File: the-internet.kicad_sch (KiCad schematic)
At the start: 10 parts, among them J1 POWER, J2 LOLIN-C3-MINI (L), J3 LOLIN-C3-MINI (R), Q1 DMP2004K, Q2 DMP2004K

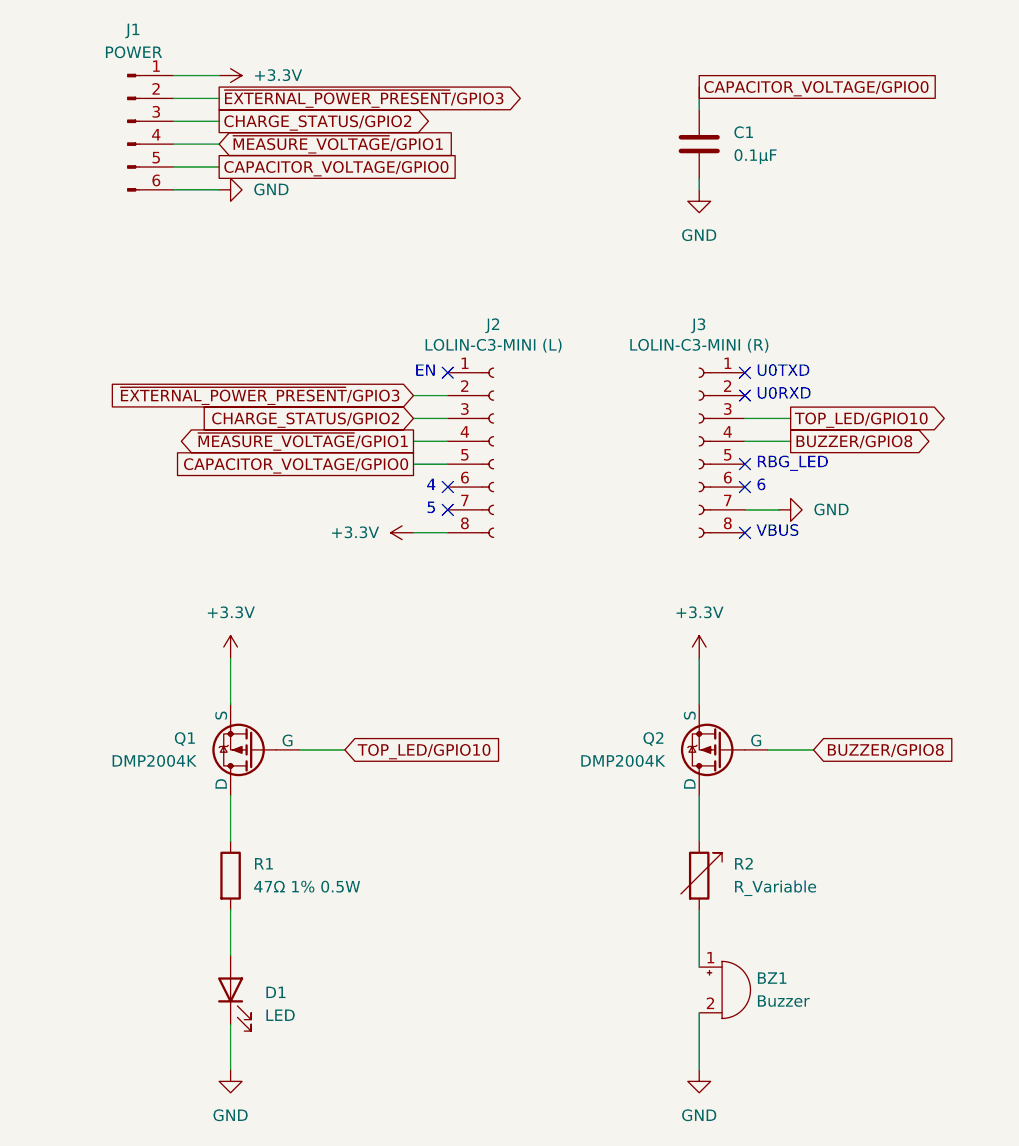
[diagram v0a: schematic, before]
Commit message: Remove ADC divider control
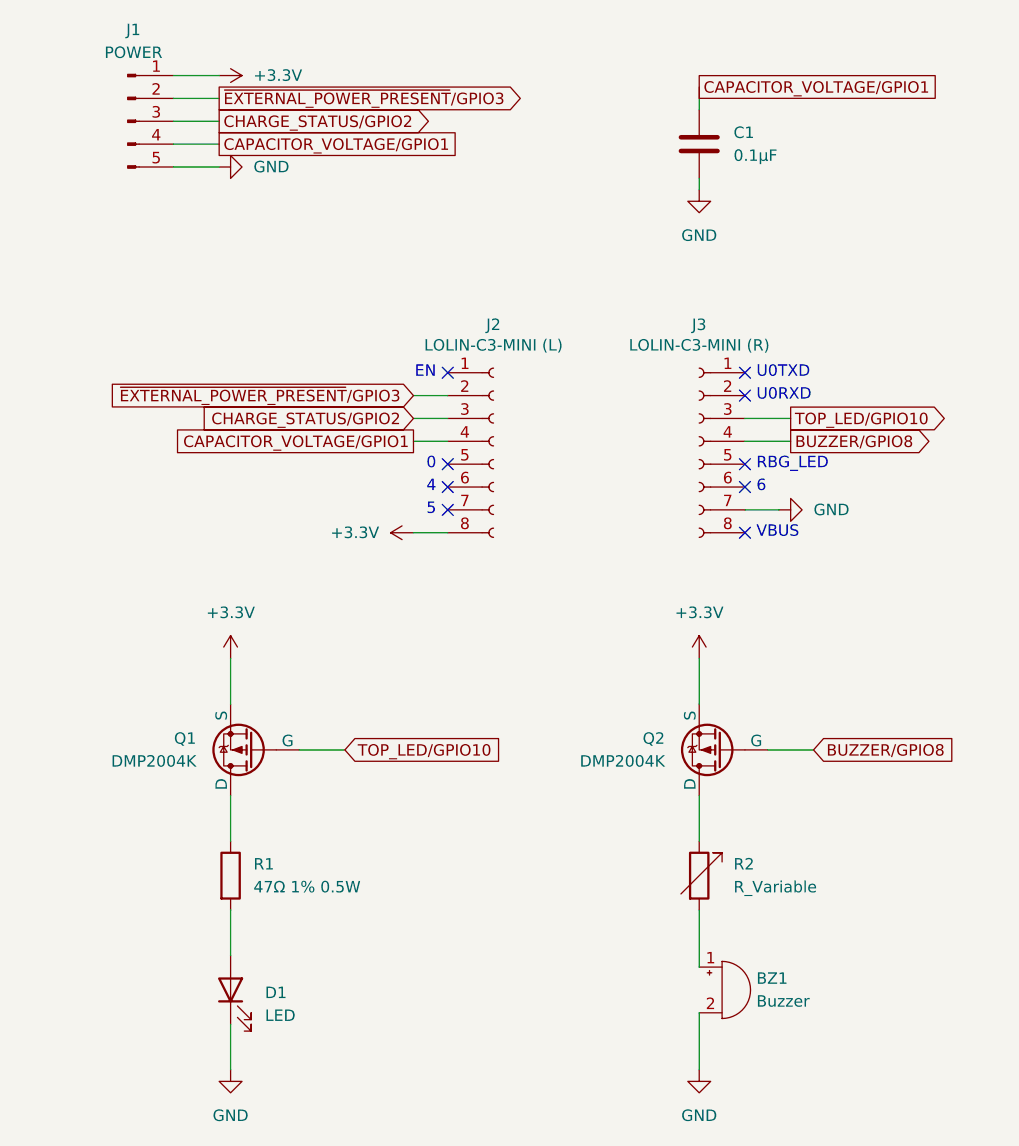
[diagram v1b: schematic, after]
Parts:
- J1: footprint Connector_PinHeader_2.54mm:PinHeader_1x06_P2.54mm_Vertical -> Connector_PinHeader_2.54mm:PinHeader_1x05_P2.54mm_Vertical; symbol Connector:Conn_01x06_Pin -> Connector:Conn_01x05_Pin
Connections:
- net GND: now also J1.5 (Pin_5); no longer J1.6 (Pin_6)
- removed net CAPACITOR_VOLTAGE/GPIO0: C1.1, J1.5 (Pin_5), J2.5 (Pin_5)
- net ~{MEASURE_VOLTAGE}/GPIO1 renamed CAPACITOR_VOLTAGE/GPIO1
- net CAPACITOR_VOLTAGE/GPIO1: now also C1.1
- no-connect marks 8 -> 9
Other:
- note added: "0"
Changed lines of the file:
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@@
+		)
+	)
+	(text "0"
+		(exclude_from_sim no)
+		(at 43.18 57.15 0)
+		(effects
+			(font
+				(size 1.27 1.27)
+			)
+			(justify right)
 		)
 	)
@@
 		(at 77.47 59.69)
 	)
+	(no_connect
+		(at 44.45 57.15)
+	)
 	(wire
 		(pts
@@
 	(wire
 		(pts
-			(xy 13.97 26.67) (xy 19.05 26.67)
-		)
-		(stroke
-			(width 0)
-			(type default)
-		)
-	)
-	(wire
-		(pts
 			(xy 77.47 54.61) (xy 82.55 54.61)
 		)
@@
 	(wire
 		(pts
-			(xy 40.64 57.15) (xy 44.45 57.15)
-		)
-		(stroke
-			(width 0)
-			(type default)
-		)
-	)
-	(wire
-		(pts
 			(xy 20.32 119.38) (xy 20.32 124.46)
 		)
@@
 		)
 	)
-	(global_label "CAPACITOR_VOLTAGE{slash}GPIO0"
+	(global_label "CAPACITOR_VOLTAGE{slash}GPIO1"
 		(shape passive)
 		(at 72.39 15.24 0)
@@
 		)
 	)
-	(global_label "CAPACITOR_VOLTAGE{slash}GPIO0"
+	(global_label "CAPACITOR_VOLTAGE{slash}GPIO1"
 		(shape passive)
-		(at 19.05 24.13 0)
+		(at 19.05 21.59 0)
 		(fields_autoplaced yes)
 		(effects
@@
 		)
 		(property "Intersheetrefs" "${INTERSHEET_REFS}"
-			(at 46.9893 24.13 0)
-			(effects
-				(font
-					(size 1.27 1.27)
-				)
-				(justify left)
-				(hide yes)
-			)
-		)
-	)
-	(global_label "CAPACITOR_VOLTAGE{slash}GPIO0"
+			(at 46.9893 21.59 0)
+			(effects
+				(font
+					(size 1.27 1.27)
+				)
+				(justify left)
+				(hide yes)
+			)
+		)
+	)
+	(global_label "CAPACITOR_VOLTAGE{slash}GPIO1"
 		(shape passive)
-		(at 40.64 57.15 180)
+		(at 40.64 54.61 180)
 		(fields_autoplaced yes)
 		(effects
@@
 		)
 		(property "Intersheetrefs" "${INTERSHEET_REFS}"
-			(at 12.7007 57.15 0)
+			(at 12.7007 54.61 0)
 			(effects
 				(font
@@
 				)
 				(justify right)
-				(hide yes)
-			)
-		)
-	)
-	(global_label "~{MEASURE_VOLTAGE}{slash}GPIO1"
-		(shape output)
-		(at 40.64 54.61 180)
-		(fields_autoplaced yes)
-		(effects
-			(font
-				(size 1.27 1.27)
-			)
-			(justify right)
-		)
-		(property "Intersheetrefs" "${INTERSHEET_REFS}"
-			(at 13.1015 54.61 0)
-			(effects
-				(font
-					(size 1.27 1.27)
-				)
-				(justify right)
-				(hide yes)
-			)
-		)
-	)
-	(global_label "~{MEASURE_VOLTAGE}{slash}GPIO1"
-		(shape input)
-		(at 19.05 21.59 0)
-		(fields_autoplaced yes)
-		(effects
-			(font
-				(size 1.27 1.27)
-			)
-			(justify left)
-		)
-		(property "Intersheetrefs" "${INTERSHEET_REFS}"
-			(at 46.5885 21.59 0)
-			(effects
-				(font
-					(size 1.27 1.27)
-				)
-				(justify left)
 				(hide yes)
 			)
@@
 	)
 	(symbol
-		(lib_id "Connector:Conn_01x06_Pin")
+		(lib_id "Connector:Conn_01x05_Pin")
 		(at 8.89 19.05 0)
 		(unit 1)
@@
 			)
 		)
-		(property "Footprint" "Connector_PinHeader_2.54mm:PinHeader_1x06_P2.54mm_Vertical"
+		(property "Footprint" "Connector_PinHeader_2.54mm:PinHeader_1x05_P2.54mm_Vertical"
 			(at 8.89 19.05 0)
 			(effects
@@
 			)
 		)
-		(property "Description" "Generic connector, single row, 01x06, script generated"
+		(property "Description" "Generic connector, single row, 01x05, script generated"
 			(at 8.89 19.05 0)
 			(effects
@@
 		)
 		(pin "5"
-		)
-		(pin "6"
 		)
 		(instances
@@
 	(symbol
 		(lib_id "power:GND")
-		(at 19.05 26.67 90)
+		(at 19.05 24.13 90)
 		(unit 1)
 		(exclude_from_sim no)
@@
 		(fields_autoplaced yes)
 		(property "Reference" "#PWR0101"
-			(at 25.4 26.67 0)
+			(at 25.4 24.13 0)
 			(effects
 				(font
@@
 		)
 		(property "Value" "GND"
-			(at 22.86 26.6699 90)
+			(at 22.86 24.1299 90)
 			(effects
 				(font
@@
 		)
 		(property "Footprint" ""
-			(at 19.05 26.67 0)
+			(at 19.05 24.13 0)
 			(effects
 				(font
@@
 		)
 		(property "Datasheet" ""
-			(at 19.05 26.67 0)
+			(at 19.05 24.13 0)
 			(effects
 				(font
@@
 		)
 		(property "Description" "Power symbol creates a global label with name \"GND\" , ground"
-			(at 19.05 26.67 0)
-			(effects
-				(font
+			(at 19.05 24.13 0)
+			(effects
+				(font

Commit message: Use the better SOT-23-3 footprint for Q1, Q2
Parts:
- Q1, Q2: footprint Package_TO_SOT_SMD:SOT-23 -> Package_TO_SOT_SMD:SOT-23-3
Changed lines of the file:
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@@
 			)
 		)
-		(property "Footprint" "Package_TO_SOT_SMD:SOT-23"
+		(property "Footprint" "Package_TO_SOT_SMD:SOT-23-3"
 			(at 69.85 91.44 0)
 			(effects
@@
 			)
 		)
-		(property "Footprint" "Package_TO_SOT_SMD:SOT-23"
+		(property "Footprint" "Package_TO_SOT_SMD:SOT-23-3"
 			(at 17.78 91.44 0)
 			(effects

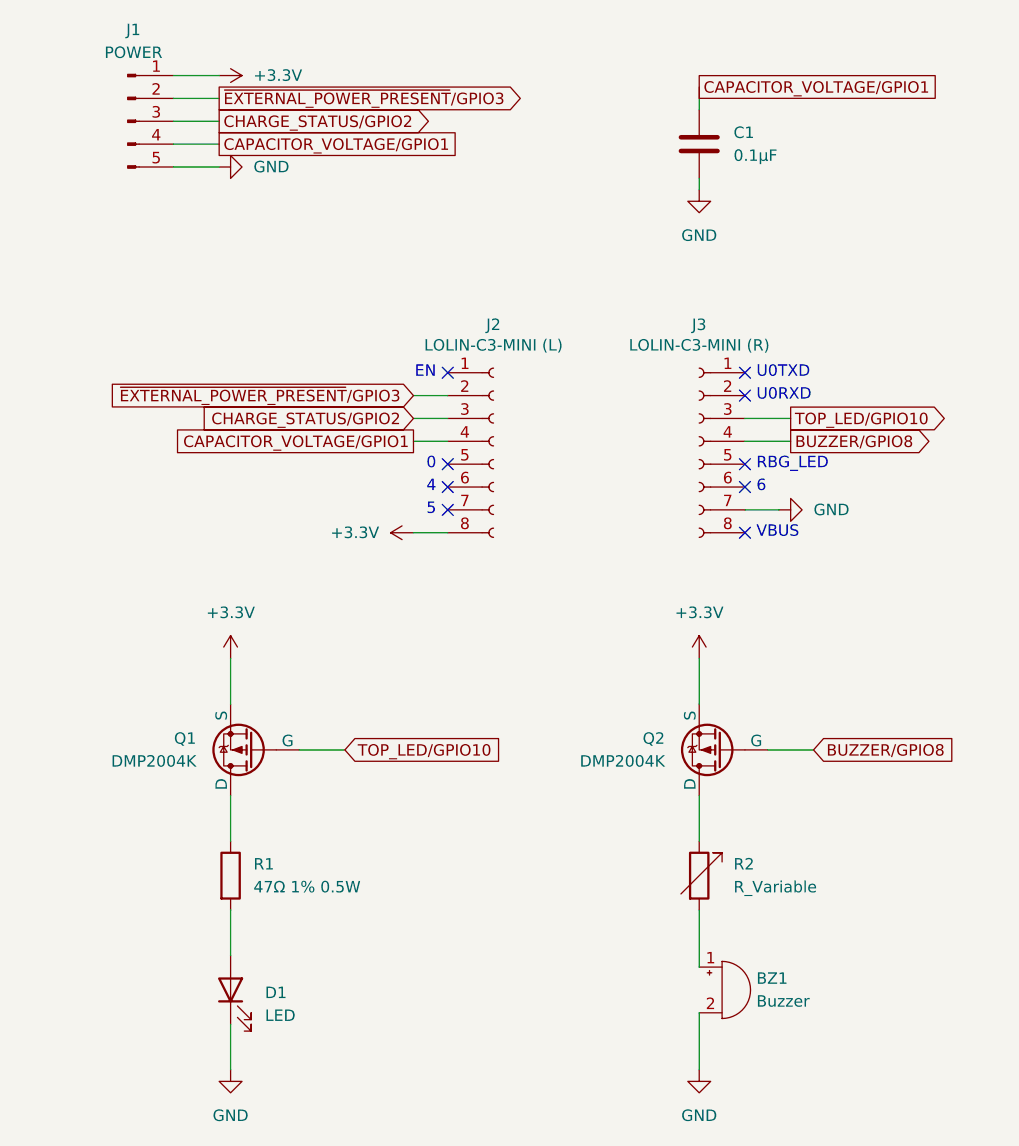
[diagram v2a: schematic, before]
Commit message: Place buzzer, remove MOSFETs
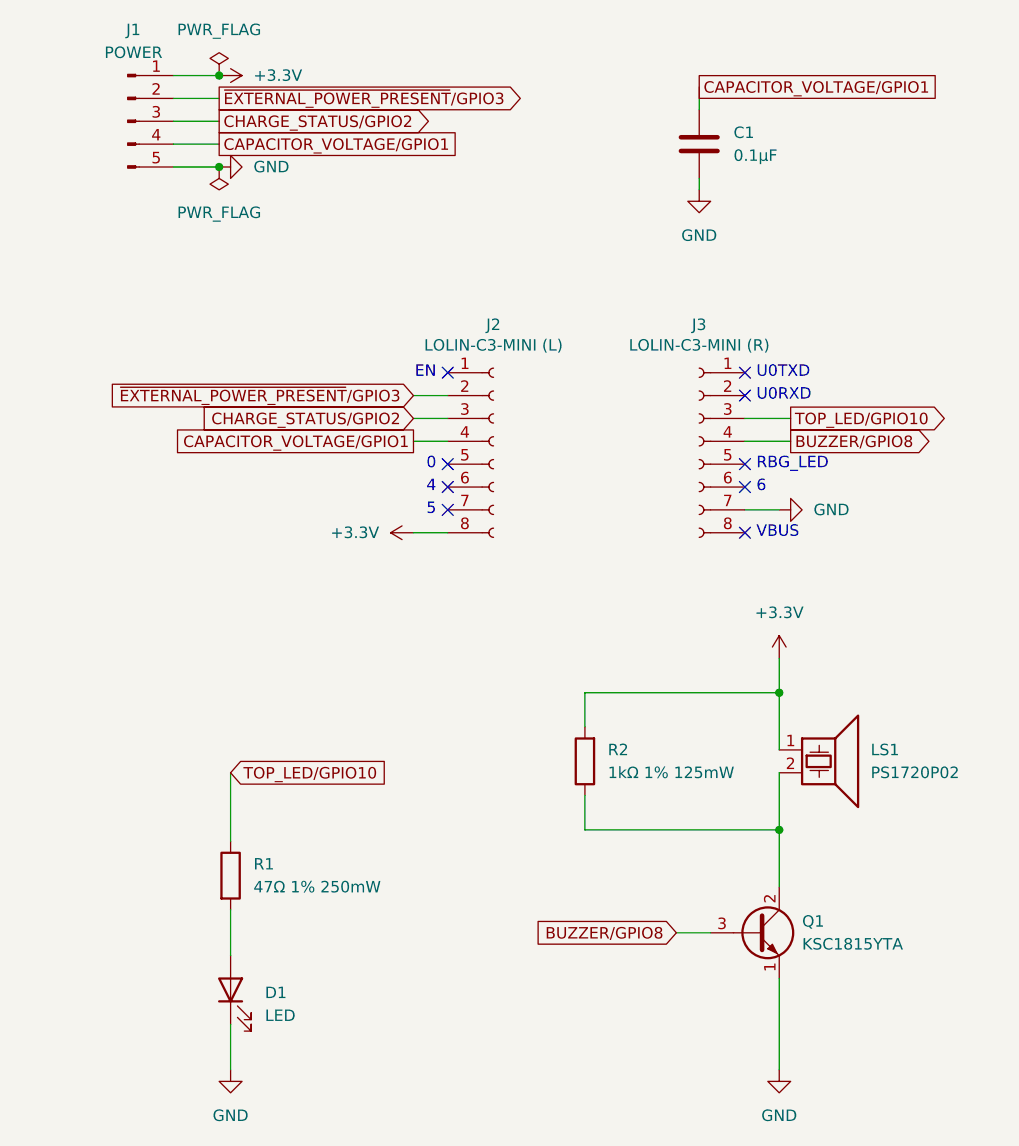
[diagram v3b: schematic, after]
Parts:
- removed Q1, Q2: DMP2004K, Package_TO_SOT_SMD:SOT-23-3, symbol Simulation_SPICE:PMOS
- added Q1: KSC1815YTA, Package_TO_SOT_THT:TO-92_Inline_Wide, symbol Transistor_BJT:Q_NPN_ECB
- LS1: renamed from BZ1; value Buzzer -> PS1720P02; footprint (none) -> the-internet:PS1720P02; symbol Device:Buzzer -> Device:Speaker_Crystal
- R1: value 47Ω 1% 0.5W -> 47Ω 1% 250mW
- R2: value R_Variable -> 1kΩ 1% 125mW; footprint (none) -> Resistor_SMD:R_0805_2012Metric_Pad1.20x1.40mm_HandSolder; symbol Device:R_Variable -> Device:R
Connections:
- net +3.3V: now also LS1.1, R2.2
- net BUZZER/GPIO8: now also Q1.3 (B)
- net GND: now also Q1.1 (E); no longer LS1.2 (-)
- net TOP_LED/GPIO10: now also R1.1
- net at R2.1: now also LS1.2, Q1.2 (C)

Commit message: Move top LED to GPIO6 because GPIO10 has a glitch on powerup
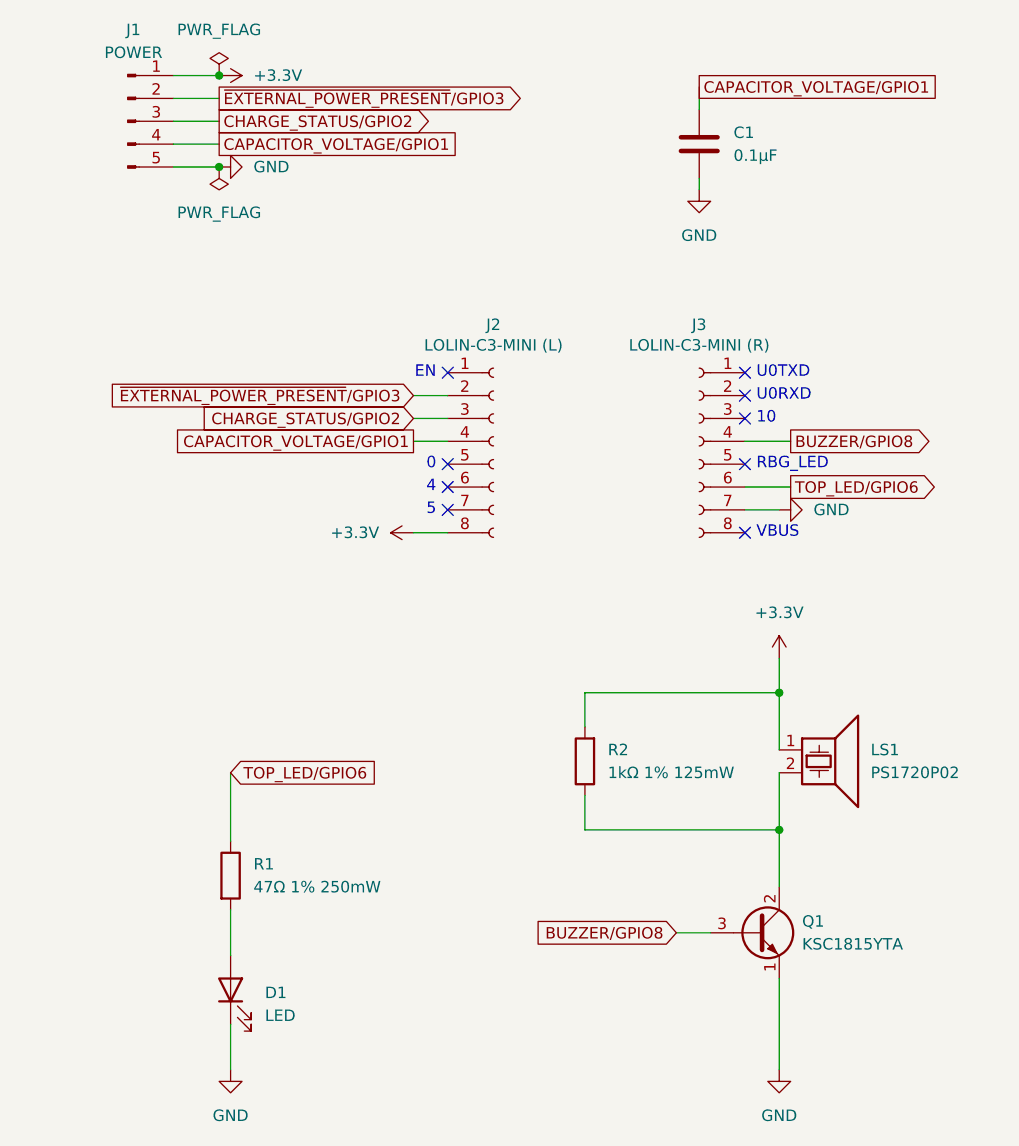
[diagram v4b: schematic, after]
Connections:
- net TOP_LED/GPIO6: now reaches J3.6 (Pin_6)
- net TOP_LED/GPIO6: now also R1.1
- net TOP_LED/GPIO10: no longer names the net of J3.3 (Pin_3)
- net TOP_LED/GPIO10: no longer R1.1
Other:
- note added: "10"
- note removed: "6"
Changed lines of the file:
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@@
 		)
 	)
-	(text "6"
+	(text "10"
 		(exclude_from_sim no)
-		(at 78.74 59.69 0)
+		(at 78.74 52.07 0)
 		(effects
 			(font
@@
 	)
 	(no_connect
+		(at 77.47 52.07)
+	)
+	(no_connect
 		(at 77.47 57.15)
 	)
@@
 	)
 	(no_connect
-		(at 77.47 59.69)
-	)
-	(no_connect
 		(at 44.45 57.15)
 	)
@@
 	(wire
 		(pts
-			(xy 82.55 52.07) (xy 77.47 52.07)
+			(xy 82.55 59.69) (xy 77.47 59.69)
 		)
 		(stroke
@@
 		)
 	)
-	(global_label "TOP_LED{slash}GPIO10"
+	(global_label "TOP_LED{slash}GPIO6"
 		(shape output)
-		(at 82.55 52.07 0)
+		(at 82.55 59.69 0)
 		(fields_autoplaced yes)
 		(effects
@@
 		)
 		(property "Intersheetrefs" "${INTERSHEET_REFS}"
-			(at 101.7428 52.07 0)
+			(at 100.5333 59.69 0)
 			(effects
 				(font
@@
 		)
 	)
-	(global_label "TOP_LED{slash}GPIO10"
+	(global_label "TOP_LED{slash}GPIO6"
 		(shape input)
 		(at 20.32 91.44 0)
@@
 		)
 		(property "Intersheetrefs" "${INTERSHEET_REFS}"
-			(at 39.5128 91.44 0)
+			(at 38.3033 91.44 0)
 			(effects
 				(font
